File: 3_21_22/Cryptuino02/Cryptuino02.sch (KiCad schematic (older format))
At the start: 24 parts, among them J1 Interface Connector, J2 USB_B_Micro, U1 CP2112, U2 ATmega88-20MU, U3 74LS02, Y1 8MHz

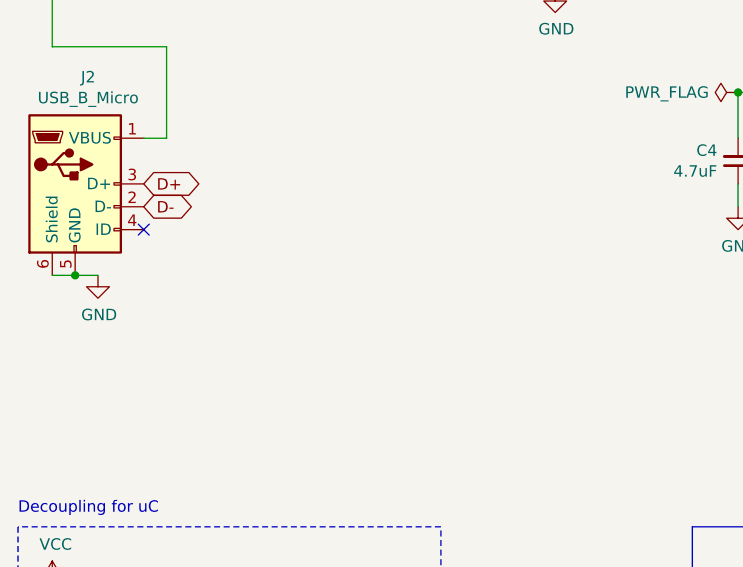
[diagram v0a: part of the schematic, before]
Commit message: Added 5to12Buck
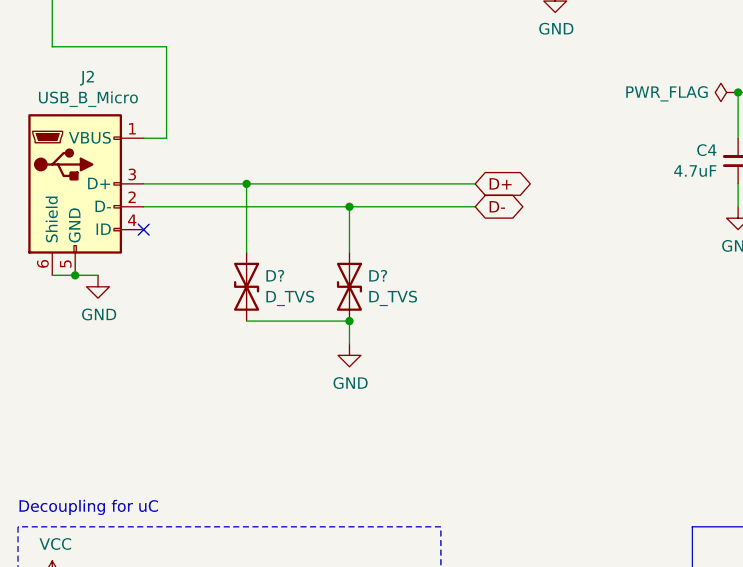
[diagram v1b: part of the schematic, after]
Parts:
- added D? (x2): D_TVS, symbol Device:D_TVS
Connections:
- net D+: now also D?.1 (A1)
- net D-: now also D?.1 (A1)
- net GND: now also D?.2 (A2), D?.2 (A2)
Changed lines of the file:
@@
 	-1   0    0    -1
 $EndComp
-Text GLabel 1250 3050 2    50   BiDi ~ 0
+Text GLabel 2700 3050 2    50   BiDi ~ 0
 D-
-Text GLabel 1250 2950 2    50   BiDi ~ 0
+Text GLabel 2700 2950 2    50   BiDi ~ 0
 D+
 $Comp
@@
 Wire Wire Line
 	5450 5500 6650 5500
+Text Notes 700  6350 0    50   ~ 0
+Decoupling for Logic & CP2112
+Wire Wire Line
+	850  7000 1300 7000
+Wire Wire Line
+	850  6800 1300 6800
+Wire Notes Line
+	2600 7450 2600 6400
+Wire Wire Line
+	1250 3050 2150 3050
+Wire Wire Line
+	1250 2950 1700 2950
+$Comp
+L Device:D_TVS D?
+U 1 1 6190F4BB
+P 1700 3400
+F 0 "D?" V 1654 3480 50  0000 L CNN
+F 1 "D_TVS" V 1745 3480 50  0000 L CNN
+F 2 "" H 1700 3400 50  0001 C CNN
+F 3 "~" H 1700 3400 50  0001 C CNN
+	1    1700 3400
+	0    1    1    0
+$EndComp
+$Comp
+L Device:D_TVS D?
+U 1 1 6190FD7A
+P 2150 3400
+F 0 "D?" V 2104 3480 50  0000 L CNN
+F 1 "D_TVS" V 2195 3480 50  0000 L CNN
+F 2 "" H 2150 3400 50  0001 C CNN
+F 3 "~" H 2150 3400 50  0001 C CNN
+	1    2150 3400
+	0    1    1    0
+$EndComp
+Wire Wire Line
+	1700 3550 2150 3550
+Wire Wire Line
+	2150 3550 2150 3650
+Connection ~ 2150 3550
+$Comp
+L power:GND #PWR?
+U 1 1 61913F7E
+P 2150 3650
+F 0 "#PWR?" H 2150 3400 50  0001 C CNN
+F 1 "GND" H 2155 3477 50  0000 C CNN
+F 2 "" H 2150 3650 50  0001 C CNN
+F 3 "" H 2150 3650 50  0001 C CNN
+	1    2150 3650
+	1    0    0    -1
+$EndComp
+Wire Wire Line
+	1700 3250 1700 2950
+Connection ~ 1700 2950
+Wire Wire Line
+	1700 2950 2700 2950
+Wire Wire Line
+	2150 3250 2150 3050
 Wire Bus Line
 	3650 4450 3650 5900
@@
 Wire Bus Line
 	5850 2250 5850 4450
-Text Notes 700  6350 0    50   ~ 0
-Decoupling for Logic & CP2112
-Wire Wire Line
-	850  7000 1300 7000
-Wire Wire Line
-	850  6800 1300 6800
-Wire Notes Line
-	2600 7450 2600 6400
+Connection ~ 2150 3050
+Wire Wire Line
+	2150 3050 2700 3050
 $EndSCHEMATC
